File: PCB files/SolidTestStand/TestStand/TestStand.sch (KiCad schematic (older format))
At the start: 48 parts, among them J1 Screw_Terminal_01x02, J2 Screw_Terminal_01x02, J3 Conn_01x08_Female, J4 Conn_01x08_Female, J5 Screw_Terminal_01x02, J6 Screw_Terminal_01x02, J7 Conn_01x08_Female, J8 Conn_01x08_Female, U1 MAX31856, U2 MAX31856, U3 MAX31856, U4 MAX31856

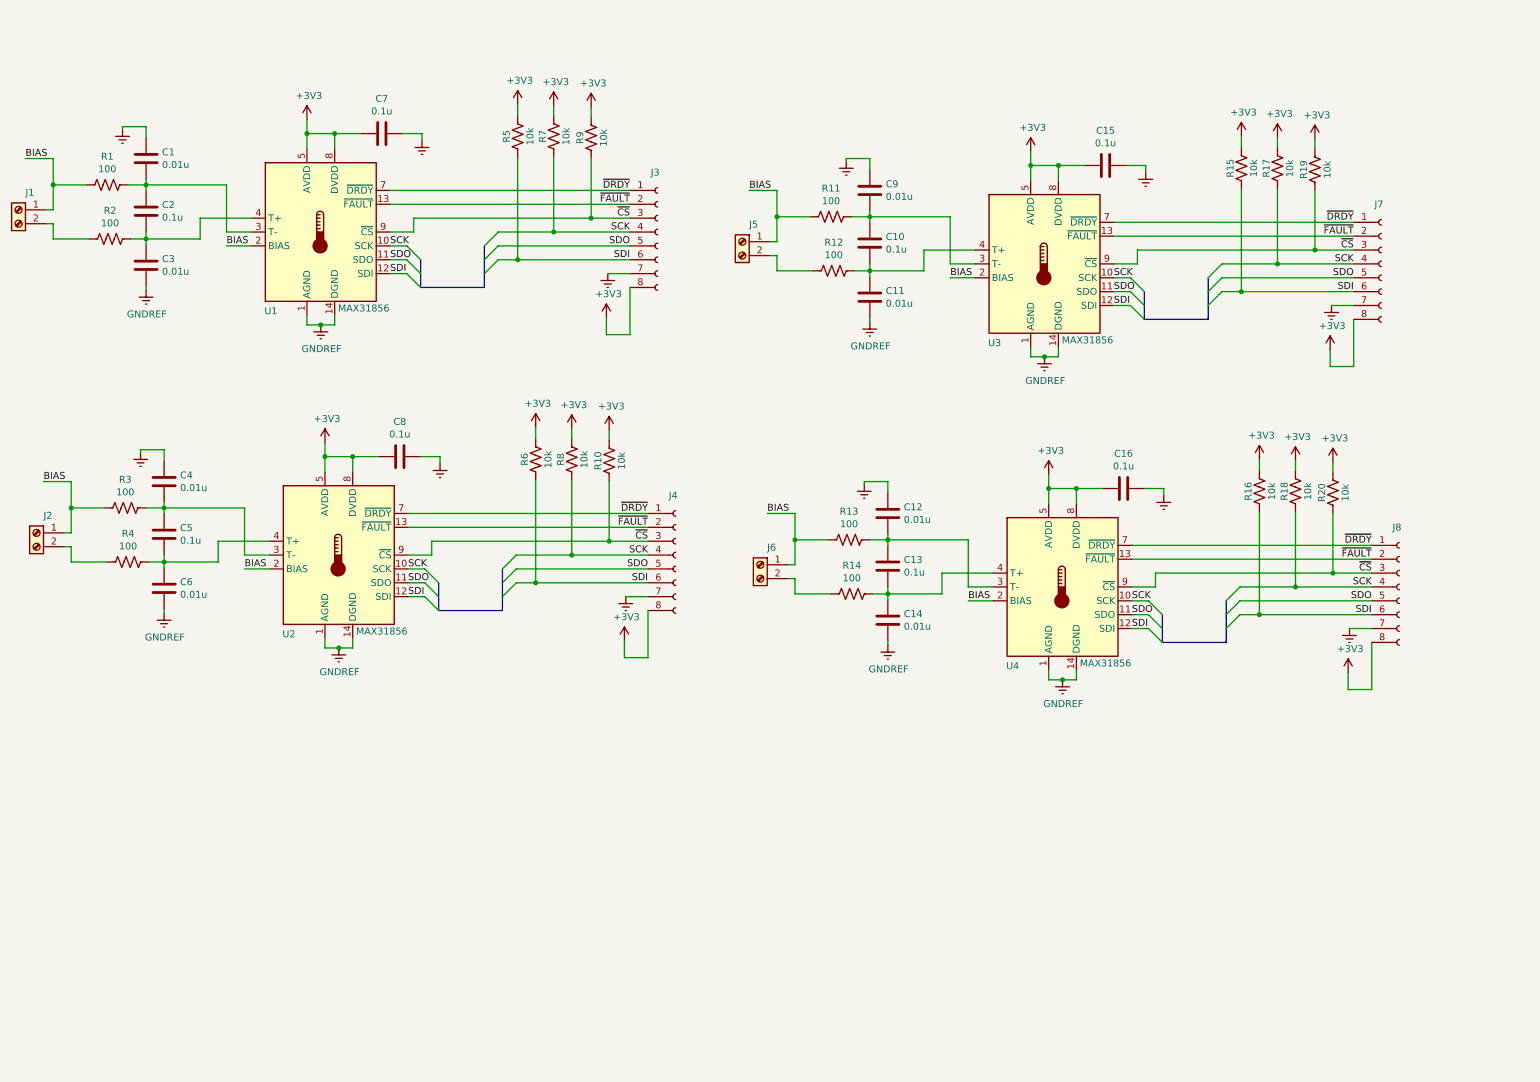
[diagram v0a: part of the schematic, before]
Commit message: 2/8/2020
-Added HX711 symbol to TestStand library
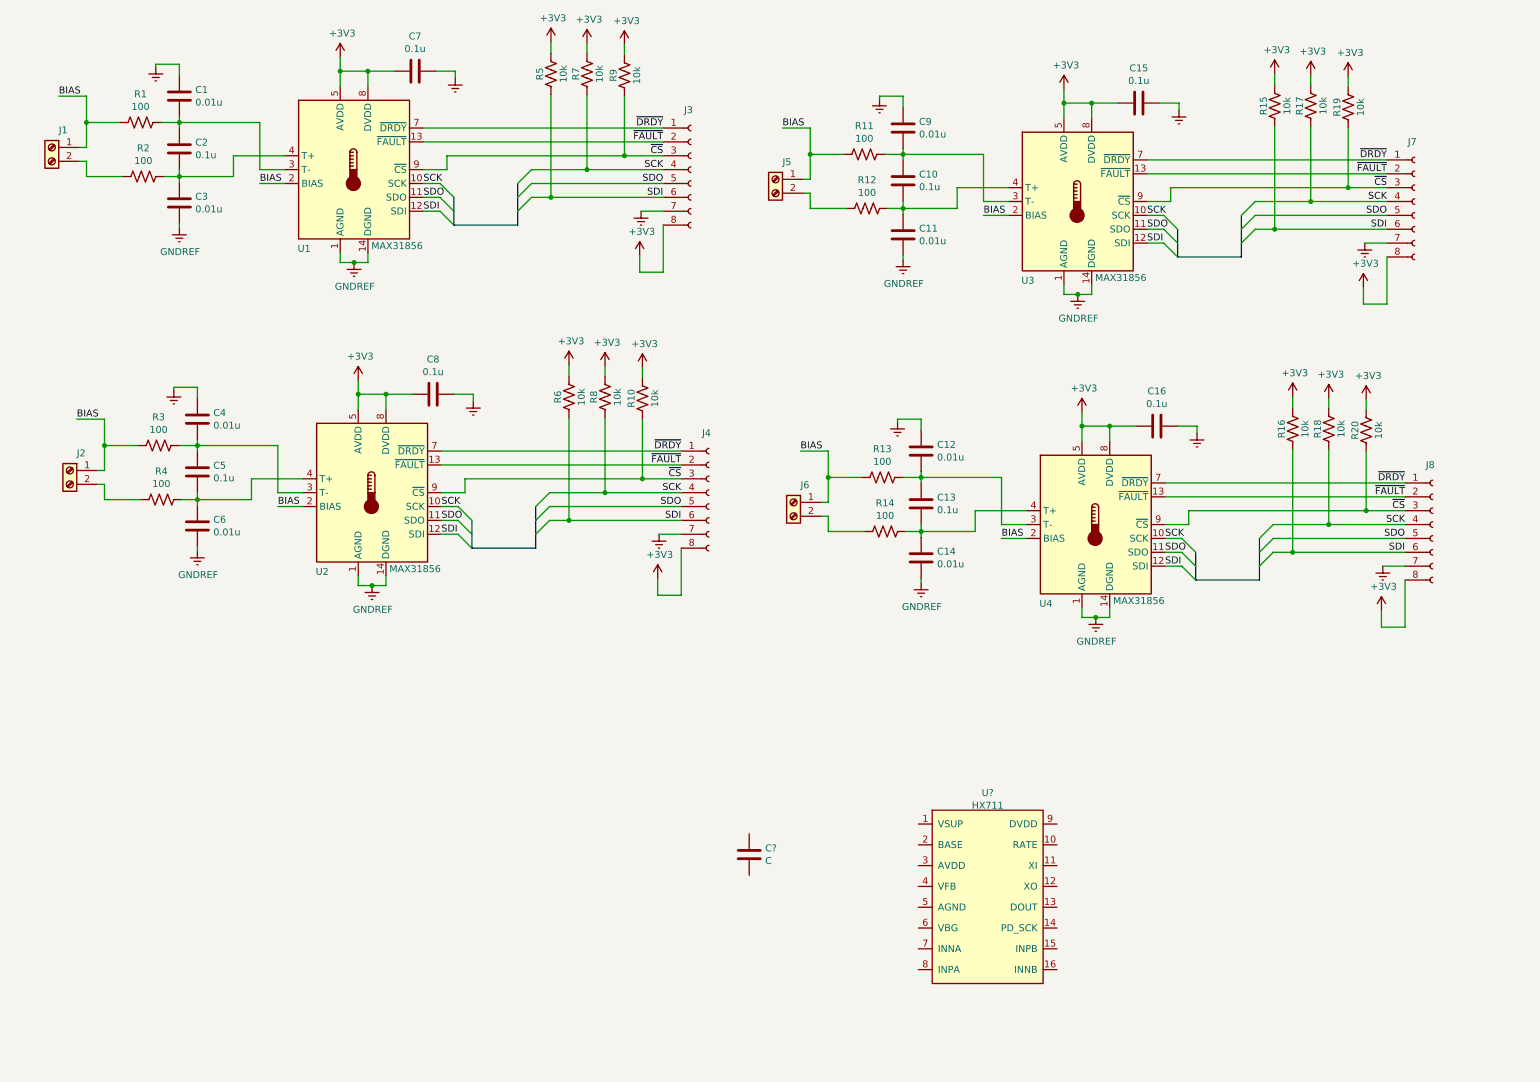
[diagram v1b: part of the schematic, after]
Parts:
- added C?: C, symbol Device:C
- added U?: HX711, symbol TestStand:HX711
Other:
- moved on the sheet: C1, C10, C11, C12, C13, C14, C15, C16, C2, C3, C4, C5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

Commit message: 2/8/2020
Schematic edits
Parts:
- removed C?: C, symbol Device:C
- added C? (x2): C_Small, symbol Device:C_Small
- added C? (x2): 0.1uF, symbol Device:C_Small
- added JP?: Jumper_NO_Small, symbol Device:Jumper_NO_Small
- added Q?: Q_PNP_BCE, symbol Device:Q_PNP_BCE
- added R?: 20k, symbol Device:R_Small
- added R?: 8k2, symbol Device:R_Small
- added R? (x2): 100, symbol Device:R_Small
- added R?: 10k, symbol Device:R_Small
- added U?: Teensy4.0, symbol teensy:Teensy4.0
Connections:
- net GNDREF: now also U?.11 (XI~), JP?.2, R?.2
- net +5V: now reaches U?.1 (VSUP)
- net +5V: now also Q?.3 (E), R?.2
- net at U?.10 (RATE): now also JP?.1, R?.1
- net at U?.2 (BASE): now also Q?.1 (B)
- net at U?.3 (AVDD~): now also Q?.2 (C), R?.1
- net at U?.4 (VFB~): now also R?.1, R?.2
- net at U?.5 (AGND~): now also C?.2
- net at U?.6 (VBG~): now also C?.1
- net at U?.7 (INNA~): now also C?.2, R?.1
- net at U?.8 (INPA~): now also C?.1, R?.1
- no-connect marks 0 -> 1
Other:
- moved on the sheet: U?

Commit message: 2/8/2020
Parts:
- added C?: 0.1uF, symbol Device:C_Small
- added U?: TMP102, Package_TO_SOT_SMD:SOT-23-6, symbol TestStand-rescue:TMP102-TestStand
- U?: symbol TestStand:HX711 -> TestStand-rescue:HX711-TestStand
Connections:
- net +3V3: now also C?.2, U?.4 (ADD0), U?.5 (V+)
- net GNDREF: now also C?.1, U?.2 (GND)
- new net ALERT: U?.3 (ALERT)
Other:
- moved on the sheet: C1, C10, C11, C12, C13, C14, C15, C16, C2, C3, C4, C5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
